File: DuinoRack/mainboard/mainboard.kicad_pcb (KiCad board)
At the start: 2 copper layers, 39.4 x 107.9 mm, 84 parts, among them J1 ISP, J2 SER, J3 Conn_02x08_Odd_Even, J4 Conn_02x05_Odd_Even, J5 Conn_MIDI, U1 MCP4822, U2 ATmega328P-P, U3 TL074, U4 TL431LP, U5 MCP6004, U6 LM1117-5.0, U7 6N138, Y1 16MHz

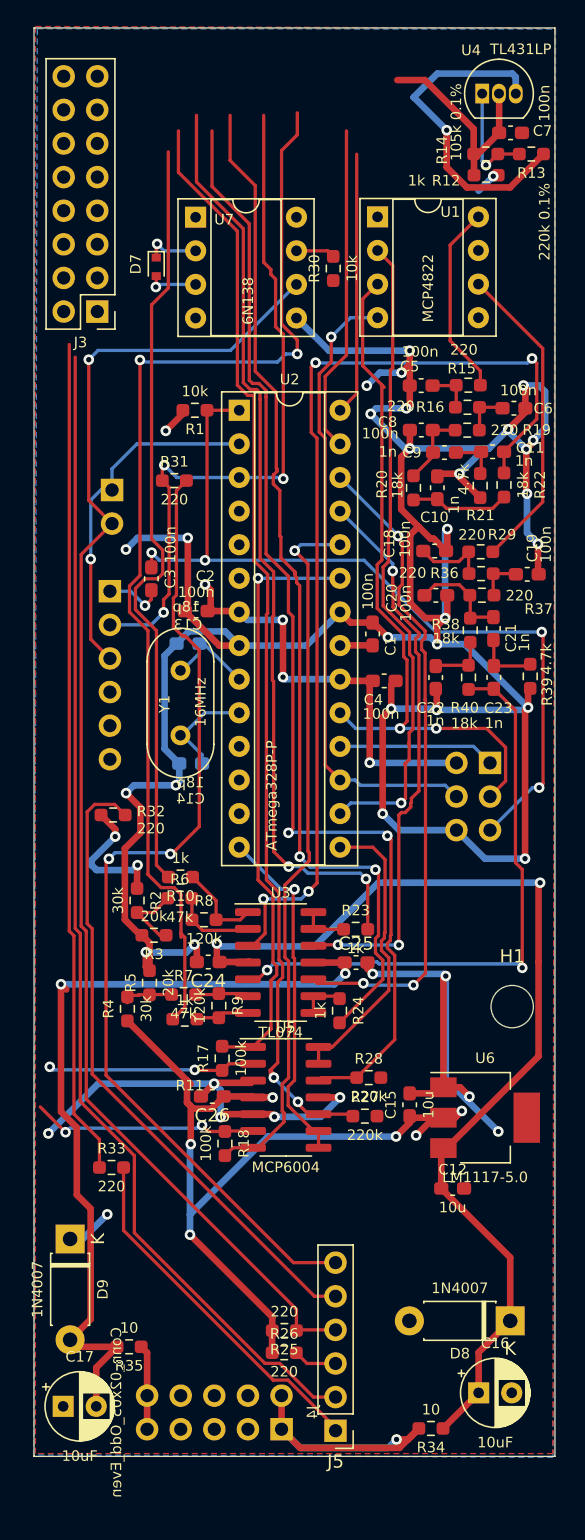
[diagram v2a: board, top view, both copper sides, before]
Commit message: Update layout with latest pcb changes
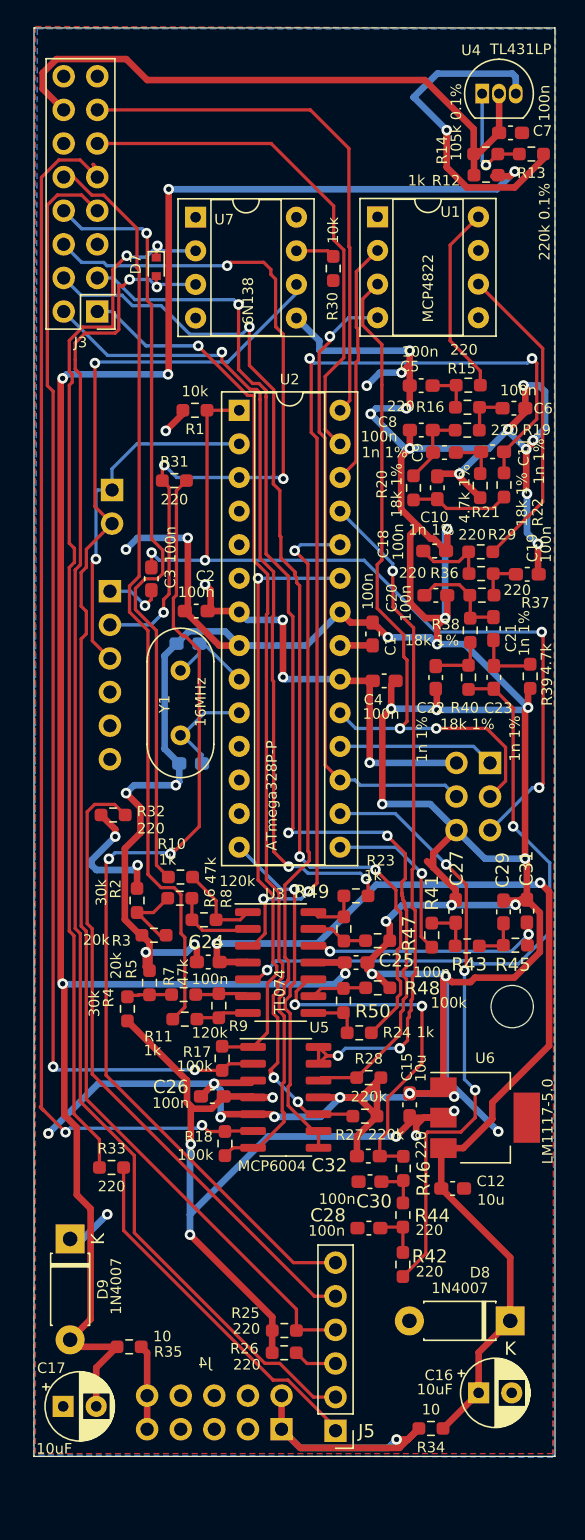
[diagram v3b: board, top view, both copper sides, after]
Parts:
- added C27: 100n, Capacitor_SMD:C_0603_1608Metric_Pad1.08x0.95mm_HandSolder, F.Cu at (124.6, 99.8)
- added C28: 100n, Capacitor_SMD:C_0603_1608Metric_Pad1.08x0.95mm_HandSolder, F.Cu at (118.0, 123.7)
- added C29: 100n, Capacitor_SMD:C_0603_1608Metric_Pad1.08x0.95mm_HandSolder, F.Cu at (128.2, 99.8)
- added C30: 100n, Capacitor_SMD:C_0603_1608Metric_Pad1.08x0.95mm_HandSolder, F.Cu at (118.1, 120.2)
- added C31: 1u, Capacitor_SMD:C_0603_1608Metric_Pad1.08x0.95mm_HandSolder, F.Cu at (130.0, 99.8)
- added C32: 1u, Capacitor_SMD:C_0603_1608Metric_Pad1.08x0.95mm_HandSolder, F.Cu at (118.0, 118.3)
- added R41: 220, Resistor_SMD:R_0603_1608Metric_Pad0.98x0.95mm_HandSolder, F.Cu at (122.8, 101.6)
- added R42: 220, Resistor_SMD:R_0603_1608Metric_Pad0.98x0.95mm_HandSolder, F.Cu at (120.6, 126.5)
- added R43: 220, Resistor_SMD:R_0603_1608Metric_Pad0.98x0.95mm_HandSolder, F.Cu at (125.5, 102.4)
- added R44: 220, Resistor_SMD:R_0603_1608Metric_Pad0.98x0.95mm_HandSolder, F.Cu at (120.6, 122.7)
- added R45: 220, Resistor_SMD:R_0603_1608Metric_Pad0.98x0.95mm_HandSolder, F.Cu at (129.1, 102.3)
- added R46: 220, Resistor_SMD:R_0603_1608Metric_Pad0.98x0.95mm_HandSolder, F.Cu at (120.6, 119.2)
- added R47: 100k, Resistor_SMD:R_0603_1608Metric_Pad0.98x0.95mm_HandSolder, F.Cu at (118.7, 102.0)
- added R48: 100k, Resistor_SMD:R_0603_1608Metric_Pad0.98x0.95mm_HandSolder, F.Cu at (118.7, 105.6)
- added R49: 75k, Resistor_SMD:R_0603_1608Metric_Pad0.98x0.95mm_HandSolder, F.Cu at (116.1, 101.1)
- added R50: 75k, Resistor_SMD:R_0603_1608Metric_Pad0.98x0.95mm_HandSolder, F.Cu at (116.1, 106.5)
- C10, C11, C21, C22, C23, C9: value 1n -> 1n 1%
- R20, R22, R38, R40: value 18k -> 18k 1%
- R21: value 4.7k -> 4.7k 1%
- moved R23 2.53 mm to (117.0, 98.6)
- moved R24 2.24 mm to (117.3, 109.0), turned to 0 degrees
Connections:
- U2 pad 15: /IN2_INT -> /OUT1_INT
- U2 pad 16: /CS -> /OUT2_INT
- U2 pad 25: /OUT1_INT -> /IN2_INT
- U2 pad 26: /OUT2_INT -> /CS
- U3 pad 10: /OUT2_INT -> Net-(C32-Pad2)
- U3 pad 12: /OUT1_INT -> Net-(C31-Pad2)
- U3 pad 13: Net-(R23-Pad1) -> Net-(R47-Pad1)
- U3 pad 9: Net-(R24-Pad1) -> Net-(R48-Pad1)
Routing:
- net -12V: track 65.5 -> 159.0 mm, vias 3 -> 6
- net /CV2_IN: track 17.3 -> 95.3 mm
- net /CV1_IN: track 15.9 -> 85.3 mm
- net GND: track 322.8 -> 387.0 mm, vias 39 -> 43
- net -8V: track 16.4 -> 47.7 mm
- net /IN2_INT: track 22.4 -> 53.2 mm, vias 0 -> 3
- net /CS: track 49.0 -> 18.5 mm, vias 1 -> 0
- net /OUT1_INT: track 42.8 -> 12.9 mm, vias 3 -> 1
- net Net-(C32-Pad2): track 0.00 -> 26.8 mm, vias 0 -> 2
- net /SCL: track 19.9 -> 40.3 mm
- net Net-(C31-Pad2): track 0.00 -> 19.6 mm, vias 0 -> 2
- net /OUTB: track 84.5 -> 70.0 mm, vias 2 -> 0
- net /SDA: track 24.8 -> 39.2 mm
- net Net-(D7-Pad1): track 67.3 -> 80.2 mm, vias 1 -> 2
- net /MIDI_IN_5: track 92.3 -> 103.9 mm, vias 1 -> 2
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
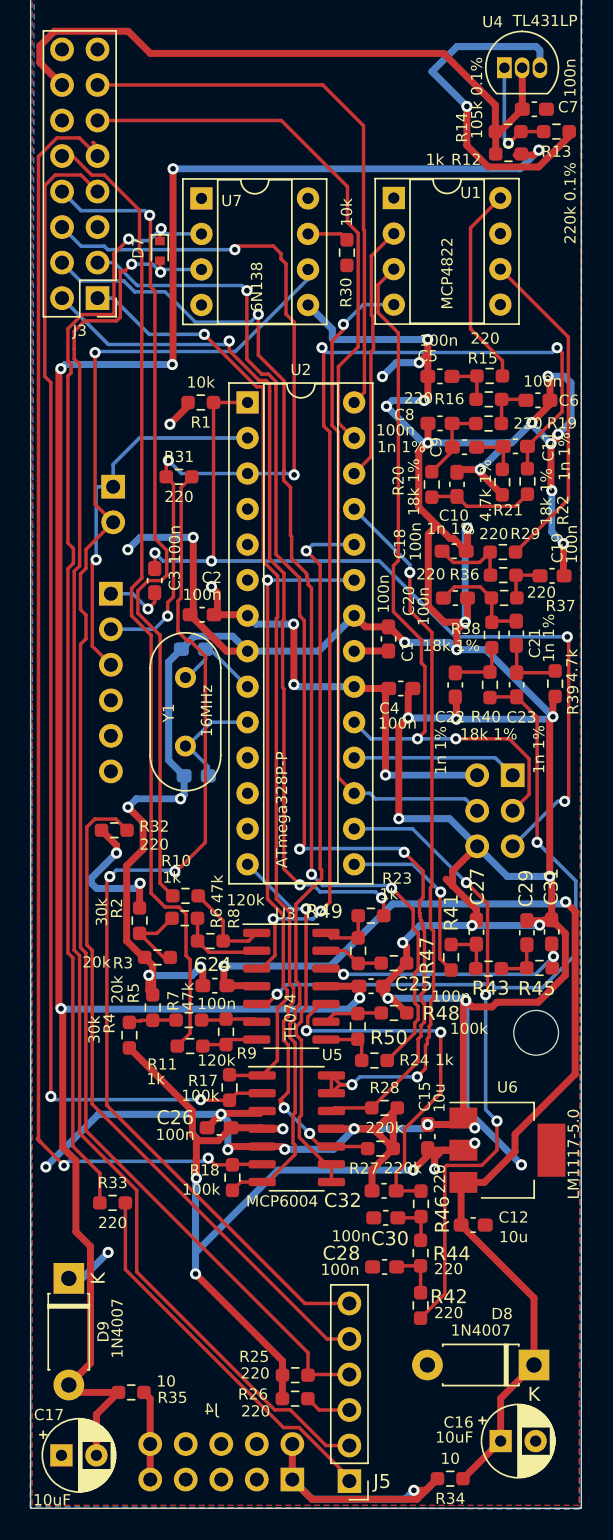
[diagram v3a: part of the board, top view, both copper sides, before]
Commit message: Add configurable input protection to enable gate IN3
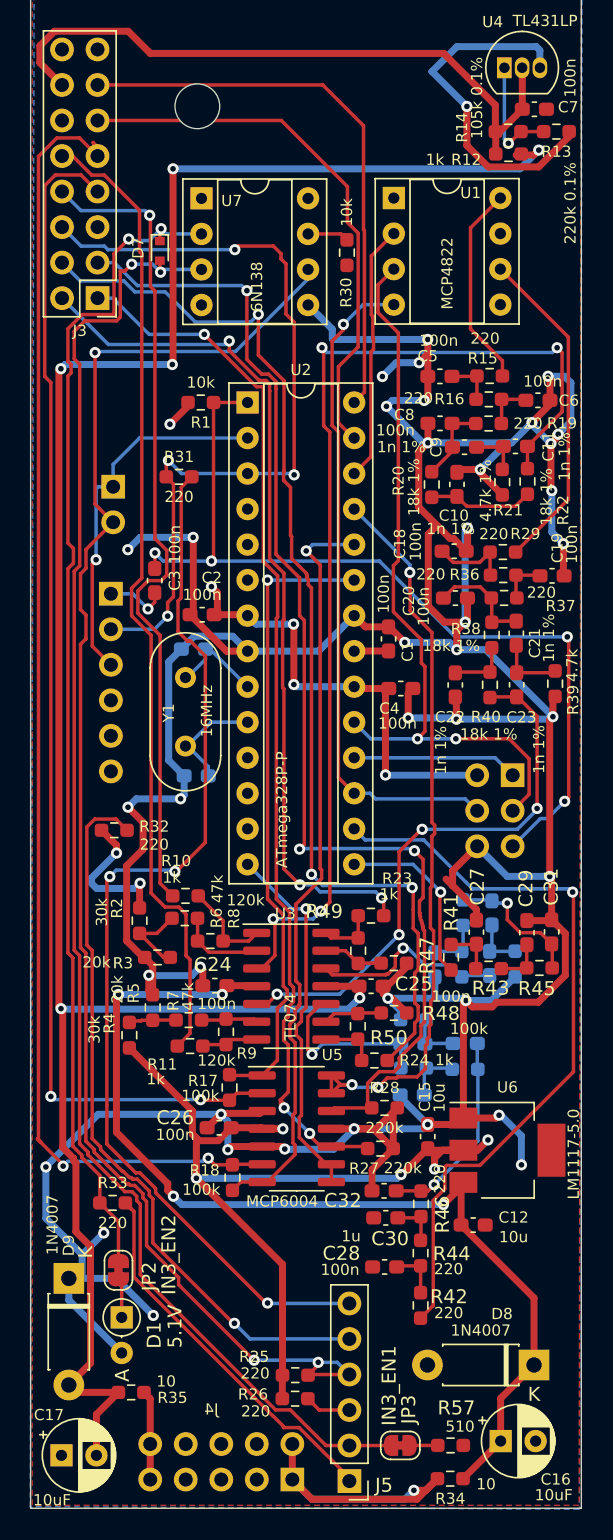
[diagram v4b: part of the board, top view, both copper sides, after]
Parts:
- added C33: 1n 1%, Capacitor_SMD:C_0603_1608Metric_Pad1.08x0.95mm_HandSolder, B.Cu at (125.7, 98.4)
- added C34: 1n 1%, Capacitor_SMD:C_0603_1608Metric_Pad1.08x0.95mm_HandSolder, B.Cu at (123.8, 107.7)
- added C35: 1n 1%, Capacitor_SMD:C_0603_1608Metric_Pad1.08x0.95mm_HandSolder, B.Cu at (121.6, 102.1)
- added C36: 1n 1%, Capacitor_SMD:C_0603_1608Metric_Pad1.08x0.95mm_HandSolder, B.Cu at (120.0, 111.4)
- added C37: 1n 1%, Capacitor_SMD:C_0603_1608Metric_Pad1.08x0.95mm_HandSolder, B.Cu at (125.5, 102.0)
- added C38: 1n 1%, Capacitor_SMD:C_0603_1608Metric_Pad1.08x0.95mm_HandSolder, B.Cu at (120.0, 107.8)
- added D1: 5.1V, Diode_THT:D_DO-35_SOD27_P2.54mm_Vertical_AnodeUp, F.Cu at (99.2, 127.3)
- added JP2: IN3_EN2, Jumper:SolderJumper-2_P1.3mm_Bridged_RoundedPad1.0x1.5mm, F.Cu at (99.0, 124.0)
- added JP3: IN3_EN1, Jumper:SolderJumper-2_P1.3mm_Bridged_RoundedPad1.0x1.5mm, F.Cu at (119.1, 136.5)
- added R51: 15k 1%, Resistor_SMD:R_0603_1608Metric_Pad0.98x0.95mm_HandSolder, B.Cu at (123.6, 98.4)
- added R52: 15k 1%, Resistor_SMD:R_0603_1608Metric_Pad0.98x0.95mm_HandSolder, B.Cu at (123.8, 109.6)
- added R53: 3.9k 1%, Resistor_SMD:R_0603_1608Metric_Pad0.98x0.95mm_HandSolder, B.Cu at (127.3, 102.1)
- added R54: 3.9k 1%, Resistor_SMD:R_0603_1608Metric_Pad0.98x0.95mm_HandSolder, B.Cu at (120.1, 106.0)
- added R55: 15k 1%, Resistor_SMD:R_0603_1608Metric_Pad0.98x0.95mm_HandSolder, B.Cu at (123.5, 102.1)
- added R56: 15k 1%, Resistor_SMD:R_0603_1608Metric_Pad0.98x0.95mm_HandSolder, B.Cu at (120.1, 109.5)
- added R57: 510, Resistor_SMD:R_0603_1608Metric_Pad0.98x0.95mm_HandSolder, F.Cu at (122.7, 136.5)
- C29, C30: value 100n -> 1u
- moved H1 70.5 mm to (104.6, 40.7)
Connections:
- U3 pad 10: Net-(C32-Pad2) -> Net-(U3-Pad10)
- U3 pad 12: Net-(C31-Pad2) -> Net-(U3-Pad12)
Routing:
- net Net-(U3-Pad12): track 0.00 -> 14.0 mm, vias 0 -> 1
- net Net-(U3-Pad10): track 0.00 -> 12.9 mm, vias 0 -> 1
- net Net-(C32-Pad2): track 26.8 -> 14.3 mm, vias 2 -> 1
- net Net-(C31-Pad2): track 19.6 -> 10.1 mm, vias 2 -> 1
- net /OUT2_INT: track 45.5 -> 53.9 mm, vias 3 -> 1
- net +12V: track 80.0 -> 73.0 mm, vias 2 -> 4
- net /OUTB_INT: track 46.6 -> 39.9 mm, vias 2 -> 4
- net /MIDI_THRU_5: track 102.7 -> 108.8 mm, vias 1 -> 3
- net GND: track 387.0 -> 382.0 mm, vias 43 -> 40
- net Net-(D7-Pad1): track 80.2 -> 84.9 mm
- net Net-(C36-Pad1): track 0.00 -> 3.87 mm
- net Net-(C35-Pad1): track 0.00 -> 3.86 mm
- net Net-(C34-Pad2): track 0.00 -> 3.78 mm
- net Net-(C33-Pad2): track 0.00 -> 3.78 mm
- net /MIDI_OUT_4: track 48.8 -> 52.3 mm, vias 0 -> 1
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
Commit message: Finish DuinoRack hardware, final touches on AS3340 VCO
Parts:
- removed J1: ISP, Connector_PinHeader_2.54mm:PinHeader_2x03_P2.54mm_Vertical
- added C39: 100n, Capacitor_SMD:C_0603_1608Metric_Pad1.08x0.95mm_HandSolder, F.Cu at (117.8, 44.9)
- added C40: 100n, Capacitor_SMD:C_0603_1608Metric_Pad1.08x0.95mm_HandSolder, B.Cu at (110.3, 59.3)
- added J6: Conn_02x03_Odd_Even, Connector_PinHeader_2.54mm:PinHeader_2x03_P2.54mm_Vertical, F.Cu at (124.4, 108.9)
- added R58: 330, Resistor_SMD:R_0603_1608Metric_Pad0.98x0.95mm_HandSolder, B.Cu at (114.4, 60.3)
- added R59: 100k 0.1%, Resistor_SMD:R_0603_1608Metric_Pad0.98x0.95mm_HandSolder, B.Cu at (112.2, 67.2)
- added R60: 100k 0.1%, Resistor_SMD:R_0603_1608Metric_Pad0.98x0.95mm_HandSolder, B.Cu at (112.2, 68.8)
- added U8: TL431DBZ, Package_TO_SOT_SMD:SOT-23, B.Cu at (112.1, 64.3)
- D7: value D -> 1N4148WS; footprint Diode_SMD:D_SOD-523 -> Diode_SMD:D_SOD-323_HandSoldering
- R13: value 220k 0.1% -> 200k 0.1%
- R14: value 105k 0.1% -> 100k 0.1%
- R51, R52, R55, R56: value 15k 1% -> 15k 0.1%
- R53, R54: value 3.9k 1% -> 3.9k 0.1%
- U4: value TL431LP -> TL431DBZ; footprint Package_TO_SOT_THT:TO-92_Inline -> Package_TO_SOT_SMD:SOT-23
- moved C4 15.2 mm to (104.9, 77.1), turned to 0 degrees
- moved C2 15.1 mm to (119.1, 82.2), turned to 0 degrees
- moved C27 13.6 mm to (124.5, 86.1)
- moved C29 13.6 mm to (128.1, 86.2)
- moved C31 13.6 mm to (129.9, 86.1)
- moved C33 13.6 mm to (125.6, 84.8)
- moved C35 13.6 mm to (121.5, 88.5)
- moved C37 13.6 mm to (125.4, 88.4)
- moved R41 13.6 mm to (122.7, 87.9)
- moved R43 13.6 mm to (125.3, 88.8)
- moved R45 13.6 mm to (129.0, 88.7)
- moved R51 13.6 mm to (123.5, 84.8)
- moved R53 13.6 mm to (127.2, 88.4)
- moved R55 13.6 mm to (123.4, 88.4)
- moved R52 11.7 mm to (128.8, 99.1)
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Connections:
- C2 pad 1: +5V -> +5VA
- J2 pad 2: /OUT3 -> unconnected-(J2-Pad2)
- J2 pad 3: /RX -> +5V
- J2 pad 4: +5V -> /RX
- J2 pad 5: unconnected-(J2-Pad5) -> /OUT3
- J3 pad 16: GND -> +12V
- U1 pad 1: +5V -> +5VA
- U2 pad 20: +5V -> +5VA
- U4 pad 1: Net-(R13-Pad2) -> GND
- U4 pad 2: -8V -> Net-(R13-Pad2)
- U4 pad 3: GND -> -8V
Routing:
- net GND: track 382.0 -> 479.7 mm, vias 40 -> 49
- net +12V: track 73.0 -> 167.4 mm
- net +5VA: track 0.00 -> 56.9 mm, vias 0 -> 2
- net /ENC1: track 0.00 -> 52.3 mm, vias 0 -> 3
- net /ENC1B: track 0.00 -> 51.6 mm, vias 0 -> 2
- net /ENC1A: track 0.00 -> 51.2 mm, vias 0 -> 2
- net /RESET: track 63.9 -> 19.2 mm, vias 4 -> 2
- net /ENC2A: track 0.00 -> 42.9 mm, vias 0 -> 1
- net +5V: track 106.5 -> 149.2 mm
- net /ENC2B: track 0.00 -> 41.9 mm, vias 0 -> 1
- net /ENC2: track 0.00 -> 37.4 mm, vias 0 -> 1
- net Net-(C32-Pad2): track 14.3 -> 30.7 mm, vias 1 -> 3
- net Net-(C38-Pad2): track 12.9 -> 26.5 mm, vias 1 -> 3
- net /SCK: track 53.7 -> 40.6 mm, vias 2 -> 1
- net Net-(C37-Pad2): track 14.0 -> 26.1 mm, vias 1 -> 3
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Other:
- board text added: "*"
- board text added: "* 18k 0.1% ^ 4.7k 0.1% : 1n 1%"
- board text added: "+5V"
- board text added: ":"
- board text added: "GND"
- board text added: "RST"
- board text added: "RX"
- board text added: "Remove for program"
- board text added: "TX"
- board text added: "^"

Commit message: Saving latest changes
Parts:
- added D2: 1N4148WS, Diode_SMD:D_SOD-323_HandSoldering, B.Cu at (101.3, 80.5)
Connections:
- J2 pad 3: +5V -> Net-(J2-Pad3)
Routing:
- net +5V: track 149.2 -> 162.3 mm
- net Net-(J2-Pad3): track 0.00 -> 3.35 mm
- net /OUT3: track 65.4 -> 67.2 mm
- net /RESET: track 19.2 -> 20.0 mm, vias 2 -> 3
